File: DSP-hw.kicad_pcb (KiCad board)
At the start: 4 copper layers, 164.5 x 61.5 mm, 100 parts, among them J1 NC3MAH, J2 NC3MAH, J3 NC3MAH, J4 NC3MAH, J5 XLR3_AudioJack3_Combo_Ground, J6 XLR3_AudioJack3_Combo_Ground, J7 USB_C_Receptacle_USB2.0_16P, J8 Conn_01x04_Pin, Q1 BC327, SW1 SW_Push, SW2 SW_SPST, SW3 SW_SPST, SW4 SW_SPST, SW5 SW_SPST, SW6 SW_SPST, SW7 SW_SPST, SW8 SW_Push, U1 ADAU1701, U2 CAT24C256, U3 AMS1117-3.3, U4 ESP32-S3-WROOM-2, U5 AMS1117-3.3, Y1 12.228M

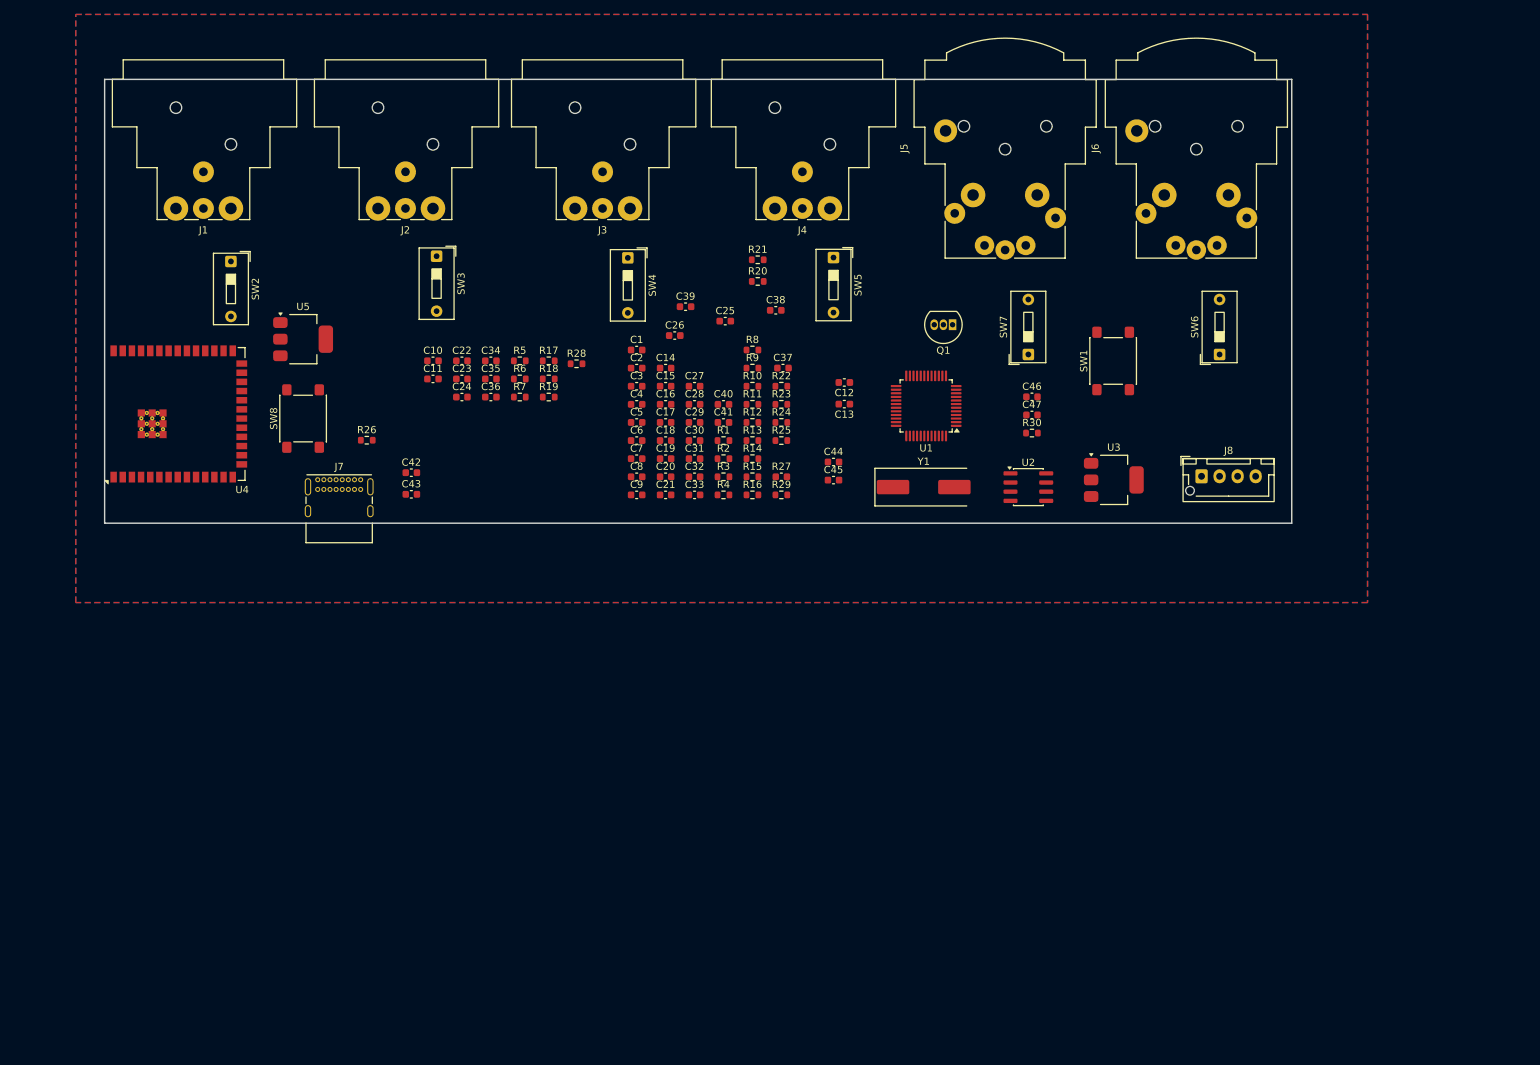
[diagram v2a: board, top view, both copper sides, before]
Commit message: sostituito micro esp32 a stm32
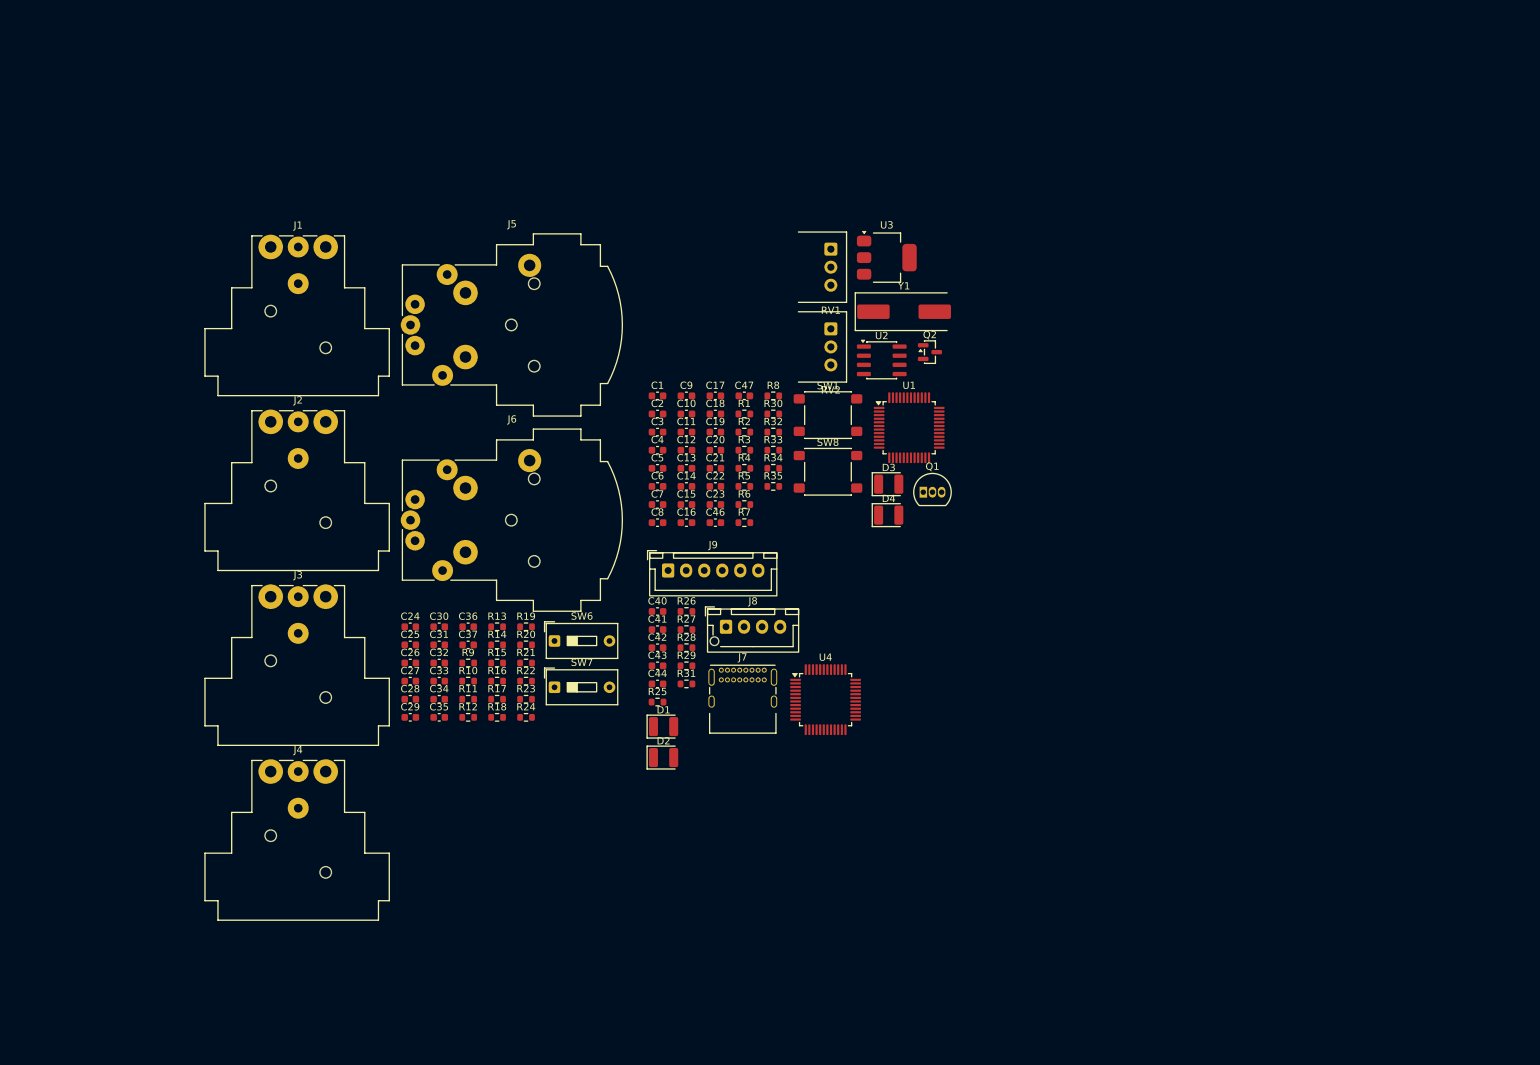
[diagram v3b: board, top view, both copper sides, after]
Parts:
- removed C38: 100n, Capacitor_SMD:C_0603_1608Metric
- removed C39: 1u, Capacitor_SMD:C_0603_1608Metric
- removed C45: 47u, Capacitor_SMD:C_0603_1608Metric
- removed SW2, SW3, SW4, SW5: SW_SPST, Button_Switch_THT:SW_DIP_SPSTx01_Slide_9.78x4.72mm_W7.62mm_P2.54mm
- removed U5: AMS1117-3.3, Package_TO_SOT_SMD:SOT-223-3_TabPin2
- added D1: LED, LED_SMD:LED_1210_3225Metric, F.Cu at (140.5, 117.7)
- added D2: LED, LED_SMD:LED_1210_3225Metric, F.Cu at (140.5, 122.0)
- added D3: LED, LED_SMD:LED_1210_3225Metric, F.Cu at (171.7, 84.1)
- added D4: LED, LED_SMD:LED_1210_3225Metric, F.Cu at (171.7, 88.4)
- added J9: Conn_01x06_Pin, Connector_JST:JST_XH_B6B-XH-A_1x06_P2.50mm_Vertical, F.Cu at (141.1, 96.1)
- added Q2: AO3400A, Package_TO_SOT_SMD:SOT-23, F.Cu at (177.4, 65.8)
- added R31: 2k2, Resistor_SMD:R_0603_1608Metric, F.Cu at (143.6, 111.8)
- added R32: 10k, Resistor_SMD:R_0603_1608Metric, F.Cu at (155.7, 76.9)
- added R33: 220, Resistor_SMD:R_0603_1608Metric, F.Cu at (155.7, 79.4)
- added R34: 2k2, Resistor_SMD:R_0603_1608Metric, F.Cu at (155.7, 81.9)
- added R35: 2k2, Resistor_SMD:R_0603_1608Metric, F.Cu at (155.7, 84.4)
- added RV1: R_Potentiometer, Potentiometer_THT:Potentiometer_Alps_RK097_Single_Horizontal, F.Cu at (163.6, 51.5)
- added RV2: R_Potentiometer, Potentiometer_THT:Potentiometer_Alps_RK097_Single_Horizontal, F.Cu at (163.6, 62.6)
- C40: value 22u -> 4.7u
- C43: value 47u -> 100n
- R27: value 10k -> 2k2; footprint Capacitor_SMD:C_0603_1608Metric -> Resistor_SMD:R_0603_1608Metric
- U4: value ESP32-S3-WROOM-2 -> STM32G473CETx; footprint RF_Module:ESP32-S3-WROOM-2 -> Package_QFP:LQFP-48_7x7mm_P0.5mm
- moved J4 110.0 mm to (86.0, 123.9), turned to 0 degrees
- moved J6 103.1 mm to (110.5, 82.1), turned to 0 degrees
- moved U4 101.4 mm to (162.9, 114.0), turned to 0 degrees
- moved SW6 100.3 mm to (125.3, 105.8), turned to 0 degrees
- moved SW7 80.2 mm to (125.3, 112.2), turned to 0 degrees
- moved J3 73.3 mm to (86.0, 99.7), turned to 0 degrees
- moved SW8 73.1 mm to (163.2, 82.4), turned to 0 degrees
- moved J5 70.8 mm to (110.5, 55.0), turned to 0 degrees
- moved J8 69.1 mm to (149.1, 103.9)
- moved R21 64.4 mm to (121.4, 108.9)
- moved C25 62.6 mm to (105.4, 106.4)
- moved J7 61.8 mm to (148.5, 109.9)
- moved R20 59.7 mm to (121.4, 106.4)
- moved C26 58.3 mm to (105.4, 108.9)
- moved C37 58.1 mm to (113.4, 106.4)
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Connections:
- net /DSP-hw/PLL_LF renamed /PLL_LF
- C26 pad 1: /Input Output filter/DAC0 -> /DAC0
- C27 pad 1: Net-(T1-AA) -> Net-(C27-Pad1)
- C28 pad 1: Net-(T1-AA) -> Net-(C27-Pad1)
- C29 pad 1: /Input Output filter/DAC1 -> /DAC1
- C30 pad 1: Net-(T2-AA) -> Net-(C30-Pad1)
- C31 pad 1: Net-(T2-AA) -> Net-(C30-Pad1)
- C32 pad 1: /Input Output filter/DAC2 -> /DAC2
- C33 pad 1: Net-(T3-AA) -> Net-(C33-Pad1)
- C34 pad 1: Net-(T3-AA) -> Net-(C33-Pad1)
- C35 pad 1: /Input Output filter/DAC3 -> /DAC3
- C36 pad 1: Net-(T4-AA) -> Net-(C36-Pad1)
- C37 pad 1: Net-(T4-AA) -> Net-(C36-Pad1)
- C42 pad 1: +5V -> +3V3
- C43 pad 1: +5V -> +3V3
- C44 pad 1: Net-(U4-3V3) -> +3V3
- J1 pad 1: Net-(SW2-A) -> GND
- J1 pad 2: Net-(T1-SA) -> Net-(C27-Pad1)
- J1 pad 3: Net-(T1-SB) -> GND
- J1 pad G: Net-(SW2-A) -> GND
- J2 pad 1: Net-(SW3-A) -> GND
- J2 pad 2: Net-(T2-SA) -> Net-(C30-Pad1)
- J2 pad 3: Net-(T2-SB) -> GND
- J2 pad G: Net-(SW3-A) -> GND
- J3 pad 1: Net-(SW4-A) -> GND
- J3 pad 2: Net-(T3-SA) -> Net-(C33-Pad1)
- J3 pad 3: Net-(T3-SB) -> GND
- J3 pad G: Net-(SW4-A) -> GND
- J4 pad 1: Net-(SW5-A) -> GND
- J4 pad 2: Net-(T4-SA) -> Net-(C36-Pad1)
- J4 pad 3: Net-(T4-SB) -> GND
- J4 pad G: Net-(SW5-A) -> GND
- J8 pad 2: /Micro/SCL -> /SCL
- J8 pad 3: /Micro/SDA -> /SDA
- R10 pad 1: /Input Output filter/ADC1 -> /ADC1
- R12 pad 1: /Input Output filter/ADC0 -> /ADC0
- R13 pad 1: Net-(T1-AA) -> Net-(C27-Pad1)
- R14 pad 1: Net-(T1-AA) -> Net-(C27-Pad1)
- R15 pad 1: Net-(T1-AA) -> Net-(C27-Pad1)
- R16 pad 1: Net-(T2-AA) -> Net-(C30-Pad1)
- R17 pad 1: Net-(T2-AA) -> Net-(C30-Pad1)
- R18 pad 1: Net-(T2-AA) -> Net-(C30-Pad1)
- R19 pad 1: Net-(T3-AA) -> Net-(C33-Pad1)
- R2 pad 2: /DSP-hw/SDA -> /SDA
- R20 pad 1: Net-(T3-AA) -> Net-(C33-Pad1)
- R21 pad 1: Net-(T3-AA) -> Net-(C33-Pad1)
- R22 pad 1: Net-(T4-AA) -> Net-(C36-Pad1)
- R23 pad 1: Net-(T4-AA) -> Net-(C36-Pad1)
- R24 pad 1: Net-(T4-AA) -> Net-(C36-Pad1)
- R27 pad 1: +3V3 -> Net-(U4-PB10)
- R27 pad 2: Net-(U4-EN) -> Net-(D2-A)
- R28 pad 2: /Micro/SDA -> /SDA
- R29 pad 2: /Micro/SCL -> /SCL
- R3 pad 2: /DSP-hw/SCL -> /SCL
- R4 pad 2: /DSP-hw/WP -> /WP
- SW8 pad 1: Net-(U4-EN) -> /WP
- U1 pad 10: unconnected-(U1-MP1-Pad10) -> /MP1
- U1 pad 11: /DSP-hw/DOUT -> /DIN
- U1 pad 15: /DSP-hw/DIN -> /DOUT
- U1 pad 16: unconnected-(U1-MP10-Pad16) -> /LRCK_2
- U1 pad 19: unconnected-(U1-MP11-Pad19) -> /BCLK_2
- U1 pad 2: /DSP-hw/ADC0 -> /ADC0
- U1 pad 21: /DSP-hw/WP -> /WP
- U1 pad 22: /DSP-hw/SDA -> /SDA
- U1 pad 23: /DSP-hw/SCL -> /SCL
- U1 pad 26: unconnected-(U1-MP9-Pad26) -> /MP9
- U1 pad 27: unconnected-(U1-MP8-Pad27) -> /MP8
- U1 pad 29: unconnected-(U1-MP2-Pad29) -> /MP2
- U1 pad 4: /DSP-hw/ADC1 -> /ADC1
- U1 pad 43: /DSP-hw/DAC3 -> /DAC3
- U1 pad 44: /DSP-hw/DAC2 -> /DAC2
- U1 pad 45: /DSP-hw/DAC1 -> /DAC1
- U1 pad 46: /DSP-hw/DAC0 -> /DAC0
- U1 pad 8: /DSP-hw/LRCLK -> /LRCK_1
- U1 pad 9: /DSP-hw/BCLK -> /BCLK_1
- U2 pad 7: /DSP-hw/WP -> /WP
- U4 pad 1: GND -> +3V3
- U4 pad 12: /Micro/SCL -> /LRCK_2
- U4 pad 13: /Micro/D- -> unconnected-(U4-PA5-Pad13)
- U4 pad 14: /Micro/D+ -> unconnected-(U4-PA6-Pad14)
- U4 pad 15: /Micro/MCLK -> unconnected-(U4-PA7-Pad15)
- U4 pad 17: /Micro/SDA -> unconnected-(U4-PB1-Pad17)
- U4 pad 19: unconnected-(U4-IO11-Pad19) -> GND
- U4 pad 2: Net-(U4-3V3) -> unconnected-(U4-PC13-Pad2)
- U4 pad 21: unconnected-(U4-IO13-Pad21) -> +3V3
- U4 pad 22: unconnected-(U4-IO14-Pad22) -> Net-(U4-PB10)
- U4 pad 23: unconnected-(U4-IO21-Pad23) -> GND
- U4 pad 24: unconnected-(U4-IO47-Pad24) -> +3V3
- U4 pad 25: unconnected-(U4-IO48-Pad25) -> Net-(U4-PB11)
- U4 pad 29: unconnected-(U4-NC-Pad29) -> /DIN
- U4 pad 3: Net-(U4-EN) -> unconnected-(U4-PC14-Pad3)
- U4 pad 30: unconnected-(U4-NC-Pad30) -> /SCL
- U4 pad 31: unconnected-(U4-IO38-Pad31) -> /SDA
- U4 pad 32: unconnected-(U4-MTCK/IO39-Pad32) -> /Micro/UART1_RX
- U4 pad 33: unconnected-(U4-MTDO/IO40-Pad33) -> /Micro/D-
- U4 pad 34: unconnected-(U4-MTDI/IO41-Pad34) -> /Micro/D+
- U4 pad 35: unconnected-(U4-MTMS/IO42-Pad35) -> GND
- U4 pad 36: unconnected-(U4-RXD0/IO44-Pad36) -> +3V3
- U4 pad 37: unconnected-(U4-TXD0/IO43-Pad37) -> /Micro/SWDIO
- U4 pad 38: unconnected-(U4-IO2-Pad38) -> /Micro/SWCLK
- U4 pad 39: unconnected-(U4-IO1-Pad39) -> /WP_M
- U4 pad 4: /Micro/BCLK -> unconnected-(U4-PC15-Pad4)
- U4 pad 40: GND -> /BCLK__2
- U4 pad 41: GND -> unconnected-(U4-PB4-Pad41)
- U4 pad 5: /Micro/LRCLK -> /LRCK_1
- U4 pad 6: /Micro/DOUT -> /BCLK_1
- U4 pad 7: /Micro/DIN -> unconnected-(U4-PG10-Pad7)
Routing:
- removed copper zone on B.Cu, net GND
- removed copper zone on F.Cu, net GND
- removed copper zone on In1.Cu, net GND
- removed copper zone on In2.Cu, net GND
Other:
- board outline removed

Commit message: aggiunto cad 3d dei connettori
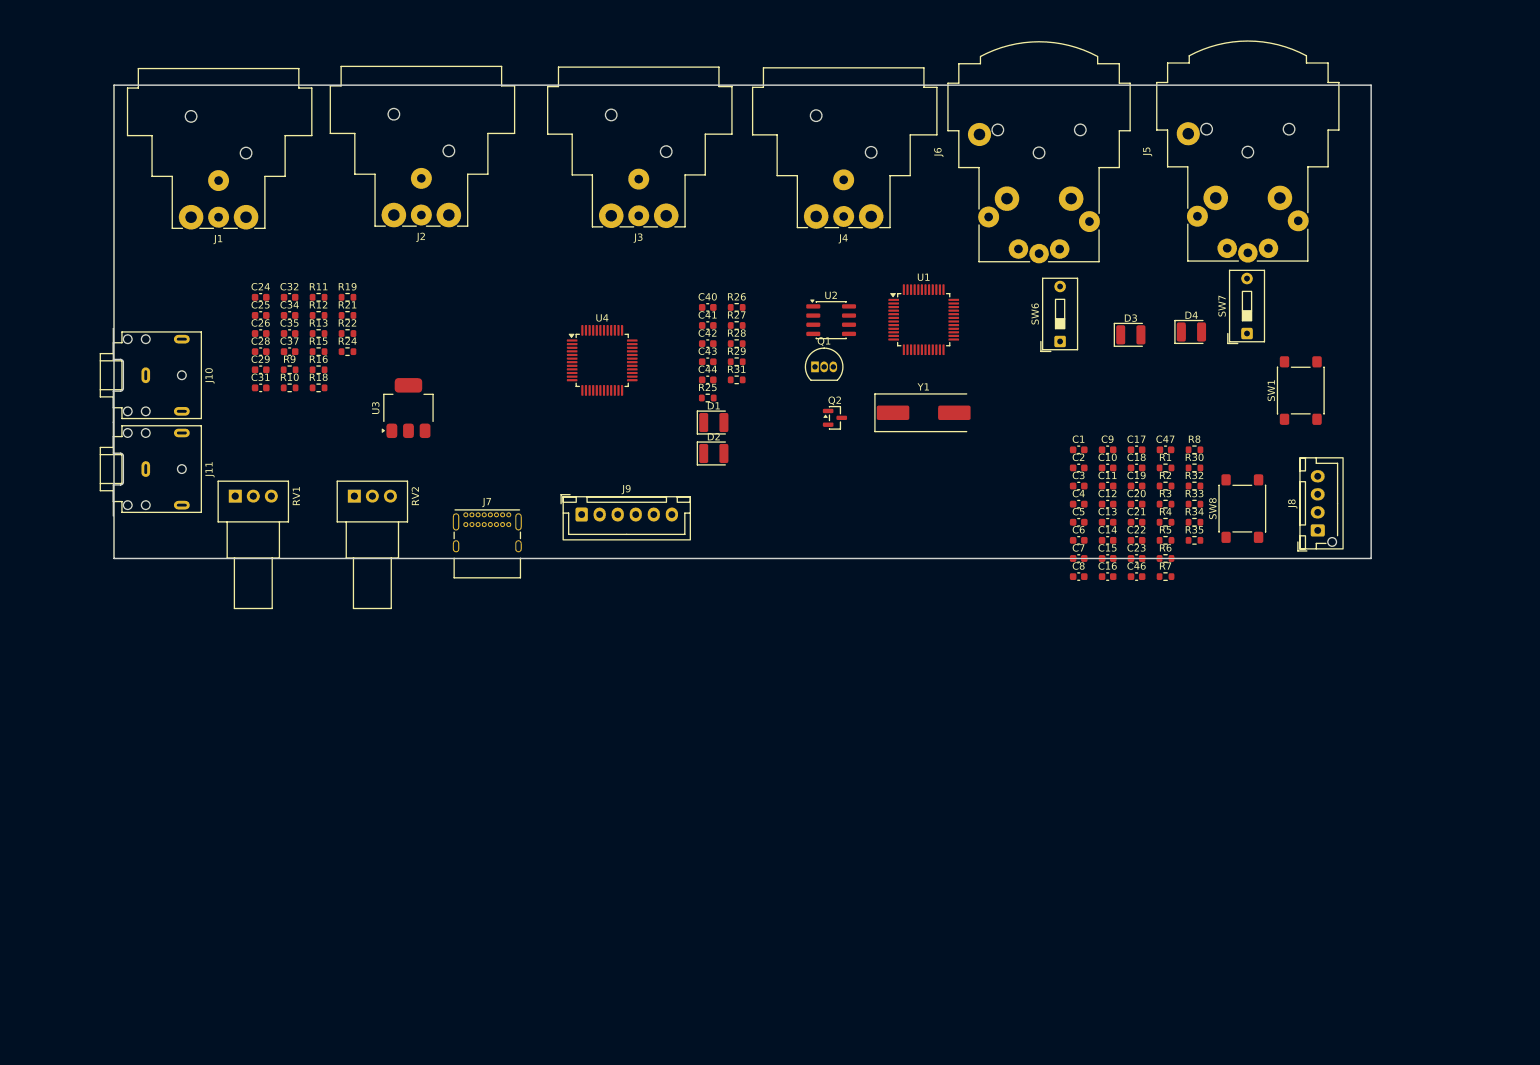
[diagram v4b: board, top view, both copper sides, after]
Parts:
- removed C27, C30, C33, C36: 56n, Capacitor_SMD:C_0603_1608Metric
- removed R14, R17, R20, R23: 47k, Resistor_SMD:R_0603_1608Metric
- added J10: AudioJack3, Connector_Audio:Jack_3.5mm_CUI_SJ1-3523N_Horizontal, F.Cu at (68.7, 69.0)
- added J11: AudioJack3, Connector_Audio:Jack_3.5mm_CUI_SJ1-3523N_Horizontal, F.Cu at (68.7, 82.0)
- C28, C31, C34, C37: value 56n -> 100n
- R15, R18, R21, R24: value 47k -> 22k
- RV1, RV2: footprint Potentiometer_THT:Potentiometer_Alps_RK097_Single_Horizontal -> Potentiometer_THT:Potentiometer_Alps_RK09Y11_Single_Horizontal
- moved J4 113.3 mm to (169.2, 47.0), turned to 180 degrees
- moved SW7 107.8 mm to (221.3, 63.2), turned to 90 degrees
- moved J5 104.3 mm to (214.4, 47.0), turned to 90 degrees
- moved RV1 89.3 mm to (81.1, 85.8), turned to 90 degrees
- moved J8 83.1 mm to (231.1, 90.5), turned to 90 degrees
- moved J6 82.8 mm to (185.5, 47.1), turned to 90 degrees
- moved SW6 81.4 mm to (195.4, 64.3), turned to 90 degrees
- moved J3 76.1 mm to (140.8, 46.9), turned to 180 degrees
- moved RV2 70.0 mm to (97.6, 85.8), turned to 90 degrees
- moved U3 69.5 mm to (105.1, 73.5), turned to 90 degrees
- moved SW1 65.6 mm to (228.8, 71.1), turned to 90 degrees
- moved R11 59.4 mm to (92.6, 58.2)
- moved R12 59.4 mm to (92.6, 60.7)
- moved C10 58.8 mm to (202.0, 81.8)
- moved C13 58.8 mm to (202.0, 89.4)
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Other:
- board outline added: 174.2 x 65.6 mm

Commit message: errore alla coca
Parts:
- added R27: 2k2, Resistor_SMD:R_0603_1608Metric, F.Cu at (134.3, 69.1)
- added R31: 2k2, Resistor_SMD:R_0603_1608Metric, F.Cu at (134.3, 71.6)
- U4: value STM32G473CETx -> STM32F411RETx; footprint Package_QFP:LQFP-48_7x7mm_P0.5mm -> Package_QFP:LQFP-64_10x10mm_P0.5mm
- moved C7 40.3 mm to (158.7, 85.1)
- moved R7 37.7 mm to (173.8, 86.5)
- moved R6 24.8 mm to (187.3, 84.4)
- moved C16 23.8 mm to (189.1, 76.9)
- moved C46 23.1 mm to (184.1, 89.6)
- moved C8 23.0 mm to (179.9, 82.7)
- moved D2 18.7 mm to (135.1, 65.7)
- moved D1 18.7 mm to (135.1, 61.4)
- moved C23 15.9 mm to (191.0, 88.9)
- moved C15 14.0 mm to (192.3, 84.2)
- moved U4 6.94 mm to (125.0, 66.5)
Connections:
- U4 pad 11: unconnected-(U4-PA3-Pad11) -> /DOUT
- U4 pad 12: /LRCK_2 -> GND
- U4 pad 13: unconnected-(U4-PA5-Pad13) -> +3V3
- U4 pad 18: unconnected-(U4-PB2-Pad18) -> GND
- U4 pad 19: GND -> +3V3
- U4 pad 20: unconnected-(U4-VREF+-Pad20) -> /BCLK_1
- U4 pad 21: +3V3 -> /LRCK_1
- U4 pad 22: Net-(U4-PB10) -> unconnected-(U4-PA6-Pad22)
- U4 pad 23: GND -> /DIN
- U4 pad 24: +3V3 -> unconnected-(U4-PC4-Pad24)
- U4 pad 25: Net-(U4-PB11) -> unconnected-(U4-PC5-Pad25)
- U4 pad 29: /DIN -> /LRCK_2
- U4 pad 3: unconnected-(U4-PC14-Pad3) -> Net-(U4-PC14)
- U4 pad 30: /SCL -> unconnected-(U4-VCAP1-Pad30)
- U4 pad 31: /SDA -> GND
- U4 pad 32: /Micro/UART1_RX -> +3V3
- U4 pad 33: /Micro/D- -> /BCLK__2
- U4 pad 34: /Micro/D+ -> unconnected-(U4-PB13-Pad34)
- U4 pad 35: GND -> unconnected-(U4-PB14-Pad35)
- U4 pad 36: +3V3 -> unconnected-(U4-PB15-Pad36)
- U4 pad 37: /Micro/SWDIO -> unconnected-(U4-PC6-Pad37)
- U4 pad 38: /Micro/SWCLK -> unconnected-(U4-PC7-Pad38)
- U4 pad 39: /WP_M -> unconnected-(U4-PC8-Pad39)
- U4 pad 4: unconnected-(U4-PC15-Pad4) -> Net-(U4-PC15)
- U4 pad 40: /BCLK__2 -> unconnected-(U4-PC9-Pad40)
- U4 pad 42: /DOUT -> /Micro/UART1_RX
- U4 pad 44: unconnected-(U4-PB7-Pad44) -> /Micro/D-
- U4 pad 45: unconnected-(U4-PB8-Pad45) -> /Micro/D+
- U4 pad 46: unconnected-(U4-PB9-Pad46) -> /Micro/SWDIO
- U4 pad 5: /LRCK_1 -> unconnected-(U4-PH0-Pad5)
- U4 pad 6: /BCLK_1 -> unconnected-(U4-PH1-Pad6)
